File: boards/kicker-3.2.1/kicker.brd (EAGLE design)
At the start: 141 x 146.1 mm, 152 parts, among them J1 B2PS-VH(LF)(SN), J2 B2PS-VH(LF)(SN), J3 B2PS-VH(LF)(SN), J4 HFW8R-1ST, J5 2-PIN_2MM-H, J6 3-PIN_2MM-H, J7 !BTN_KCK_PRE_EXT, J8 !BTN_CHP_PRE_EXT, J9 !BTN_CHG_PRE_EXT, Q1 ATP302ATPAK, Q10 BSS806NSOT-23-3, Q2 IRFS4227, Q3 IXGK400N30A3, Q4 IXGK400N30A3, Q5 BSS127, Q6 AOD1N60, Q7 BSS127, Q8 BSS127, Q9 BSS127, T1 DA203X-ALDA2034, U1 MPM3620GQV-P, U2 15V, U3 LT3751FE, U4 IX4427N, U5 AT32ATQFP44, U6 ADUM7441ARQZ-RL7, U7 ADUM7441CRQZ-RL7

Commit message: control done 3d, kicker having librarie issues
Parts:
- C16: device rcl:C0603 -> resistor:C0603
- R2, R20, R21, R22, R23, R24, R25, R26, R27, R3, R35, R38, R39, R4, R40, R42, R43, R44, R47, R48, R49, R50, R51, R52, R53: device rcl:R0603 -> resistor:R0603
- R36, R37: device rcl:R0805 -> resistor:R0603

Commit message: kicker in progress
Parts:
- C16: device resistor:C0603 -> rcl:C0603
- R2, R20, R21, R22, R23, R24, R25, R26, R27, R3, R35, R37, R38, R39, R4, R40, R42, R43, R44, R47, R48, R49, R50, R51, R52, R53: device resistor:R0603 -> rcl:R0603
- R36: device resistor:R0603 -> rcl:R0805

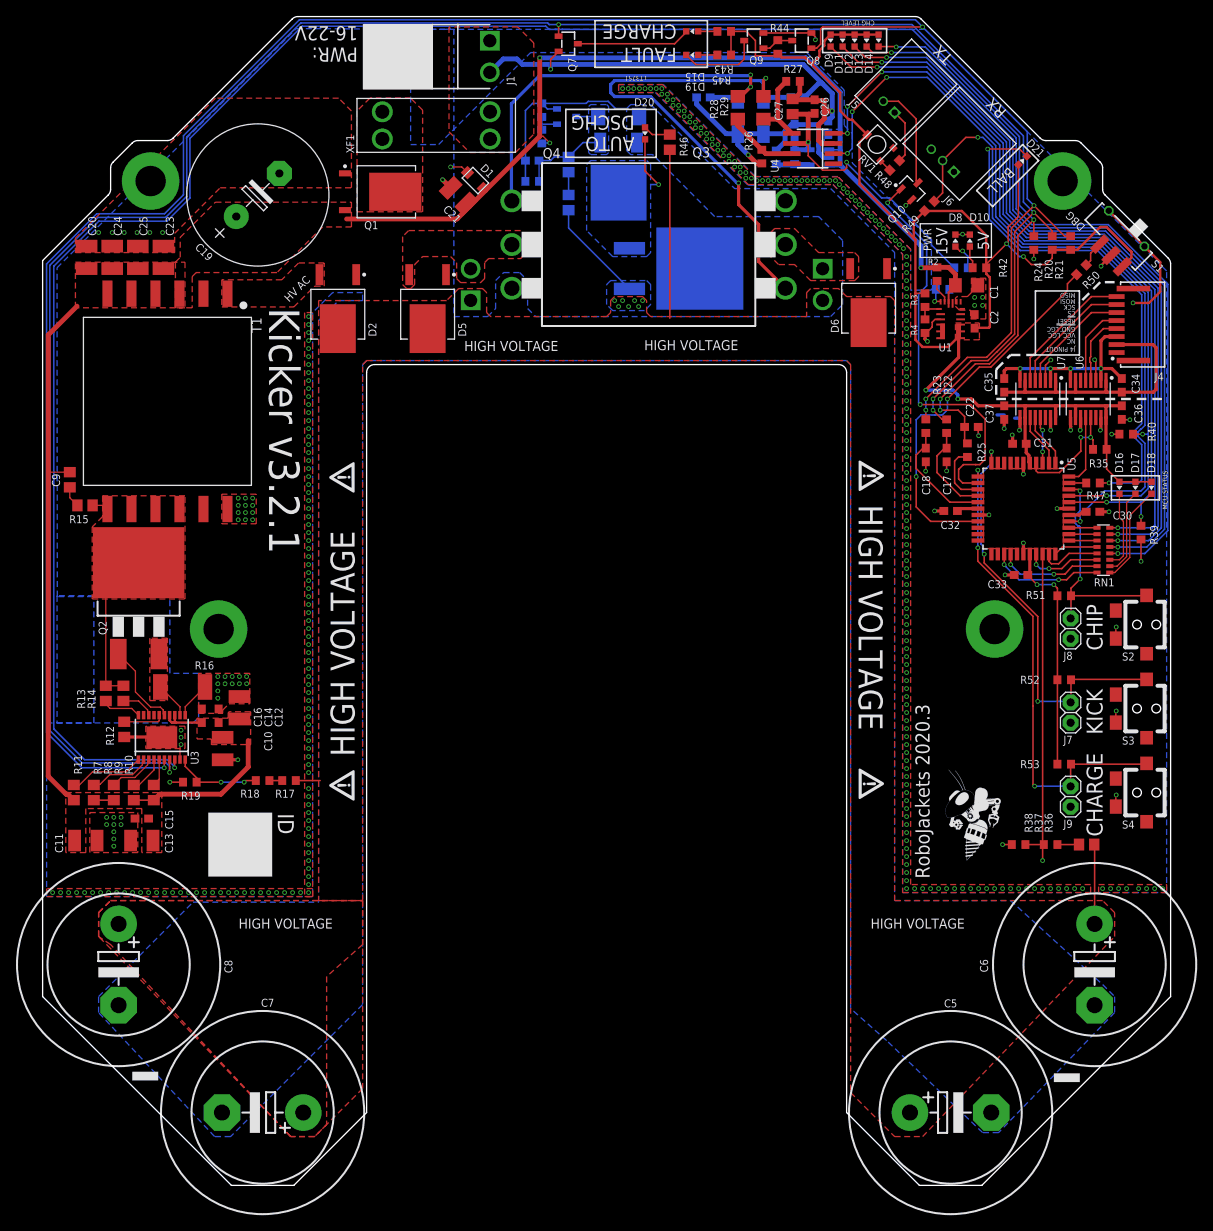
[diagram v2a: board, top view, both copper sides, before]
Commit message: radio done, kicker in progress
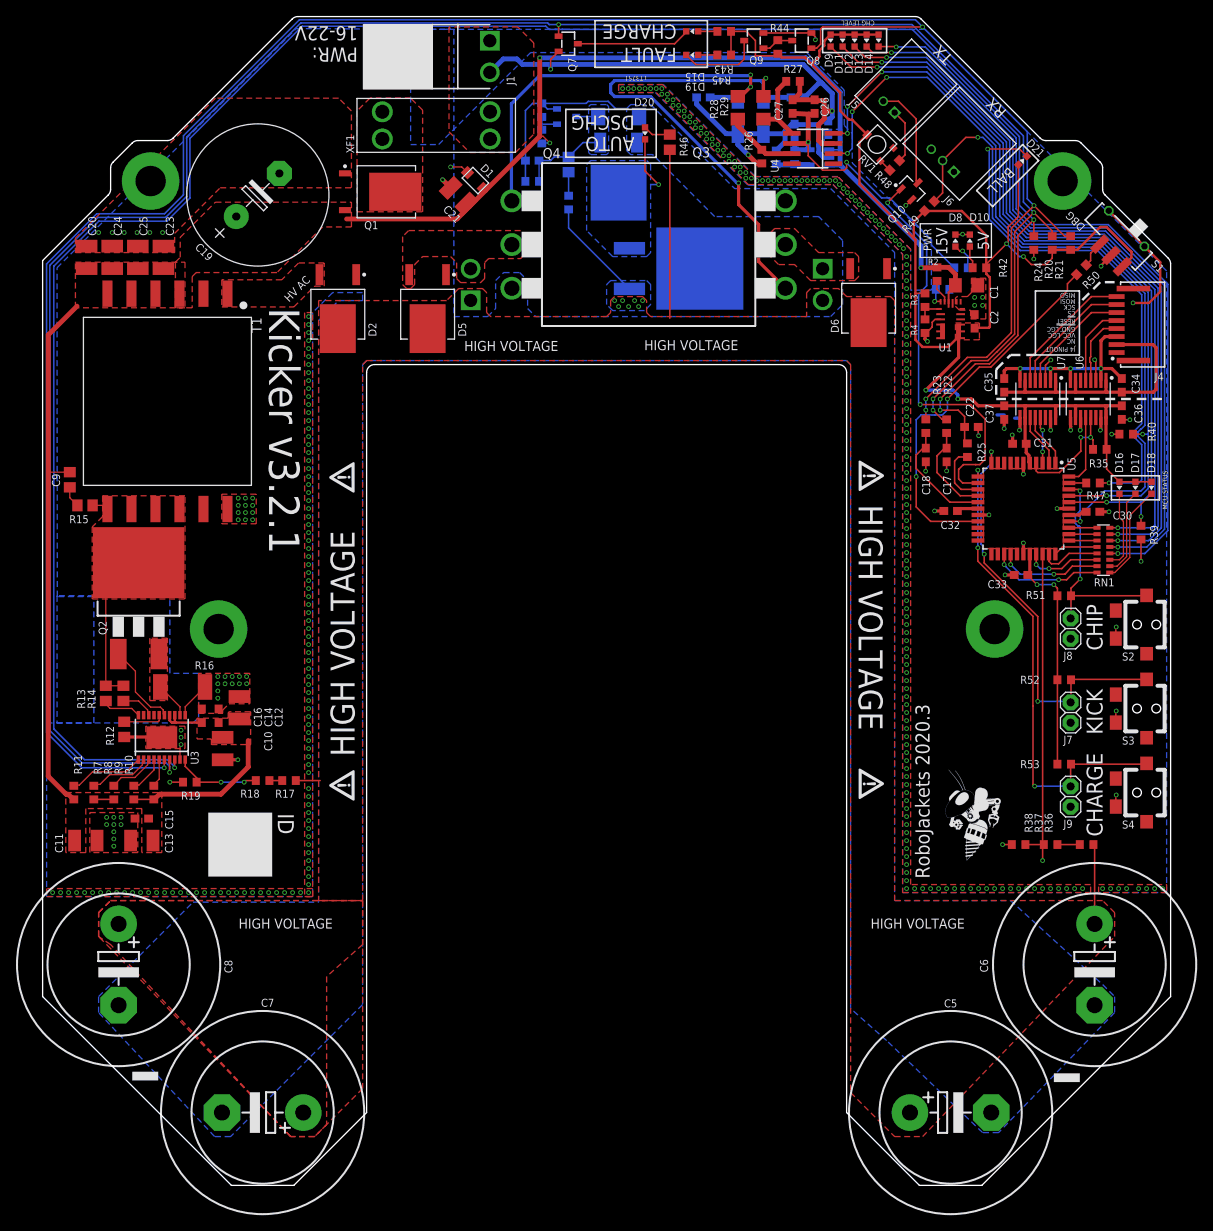
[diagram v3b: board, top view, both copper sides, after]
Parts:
- C27: device rcl:C0805 -> rcl:C0603
- C9: device resistor:C0805 -> rcl:C0805
- R10, R11, R7, R8, R9: device resistor:R0805 -> rcl:R0603
- R12, R13, R14, R15: device resistor:R0805 -> rcl:R0805
- R16: device resistor:R2512 -> rcl:R2512
- R32, R36: device rcl:R0805 -> rcl:R0603
- R5, R6: device resistor:R0603 -> rcl:R0603

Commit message: kicker done, still need breakbeam and IMU
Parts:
- C19: device rcl:E7,5-18 -> RoboJackets-Capacitors:E7,5-18
- C5, C6, C7, C8: device rcl:EB25D -> RoboJackets-Capacitors:EB25D
